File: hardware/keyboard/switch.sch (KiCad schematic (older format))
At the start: 136 parts

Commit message: I think im connecting the pins correctly on RGB...
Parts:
- added R1, R10, R11, R12, R13, R14, R2, R3, R4, R5, R6, R7, R8, R9: 10kR, symbol Device:R
- gave numbers to parts that had none: 136
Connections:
- net COL1: now also R1.1
- net COL10: now also R10.1
- net COL11: now also R11.1
- net COL12: now also R12.1
- net COL13: now also R13.1
- net COL14: now also R14.1
- net COL2: now also R2.1
- net COL3: now also R3.1
- net COL4: now also R4.1
- net COL5: now also R5.1
- net COL6: now also R6.1
- net COL7: now also R7.1
- net COL8: now also R8.1
- net COL9: now also R9.1
- new net 3.3V: R1.2, R10.2, R11.2, R12.2, R13.2, R14.2, R2.2, R3.2, R4.2, R5.2, R6.2, R7.2, R8.2, R9.2

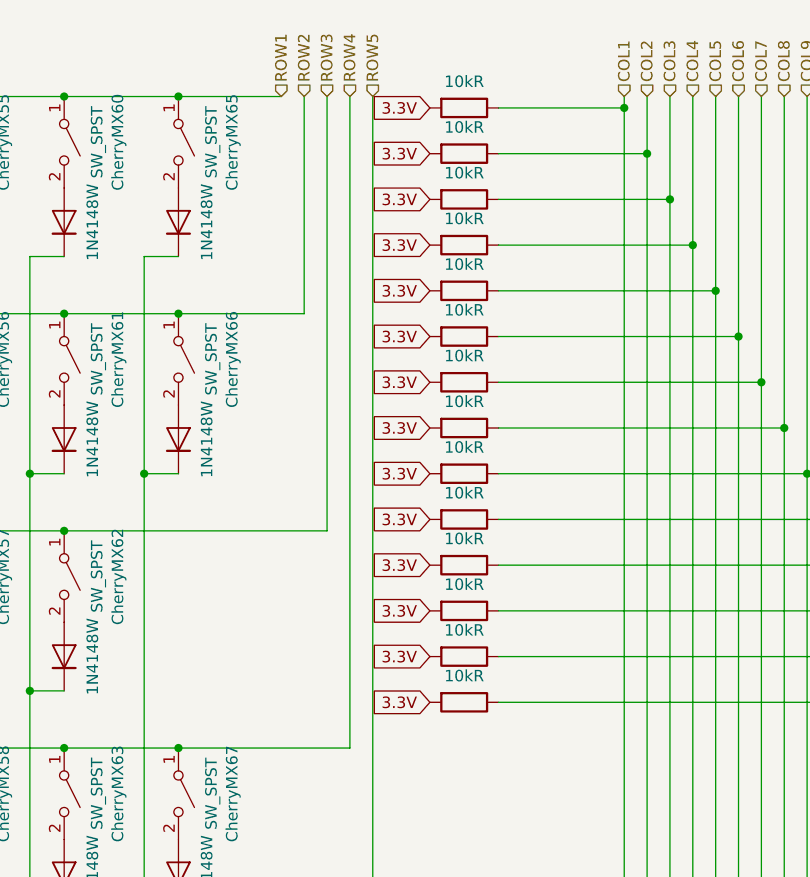
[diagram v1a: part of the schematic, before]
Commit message: switch to proper type of RGB(Common anode)
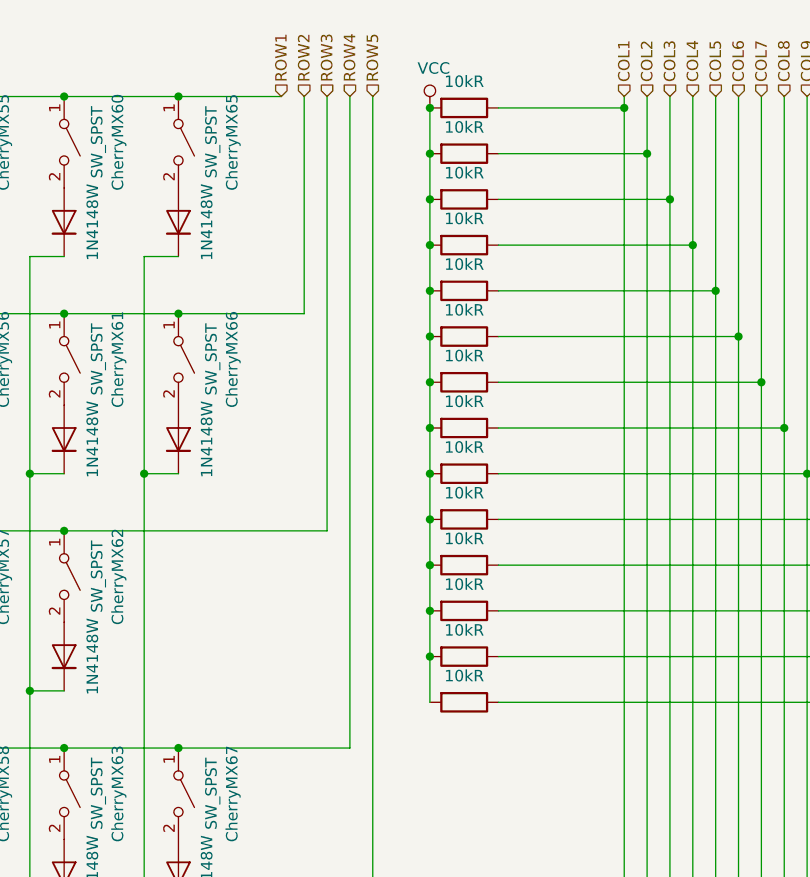
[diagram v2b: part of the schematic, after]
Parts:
- CherryMX1, CherryMX10, CherryMX11, CherryMX12, CherryMX13, CherryMX14, CherryMX15, CherryMX16, CherryMX17, CherryMX18, CherryMX19, CherryMX2, CherryMX20, CherryMX21, CherryMX22, CherryMX23, CherryMX24, CherryMX25, CherryMX26, CherryMX27, CherryMX28, CherryMX29, CherryMX3, CherryMX30, CherryMX31, CherryMX32, CherryMX33, CherryMX34, CherryMX35, CherryMX36, CherryMX37, CherryMX38, CherryMX39, CherryMX4, CherryMX40, CherryMX41, CherryMX42, CherryMX43, CherryMX44, CherryMX45, CherryMX46, CherryMX47, CherryMX48, CherryMX49, CherryMX5, CherryMX50, CherryMX51, CherryMX52, CherryMX53, CherryMX54, CherryMX55, CherryMX56, CherryMX57, CherryMX58, CherryMX59, CherryMX6, CherryMX60, CherryMX61, CherryMX62, CherryMX63, CherryMX64, CherryMX65, CherryMX66, CherryMX67, CherryMX68, CherryMX7, CherryMX8, CherryMX9: footprint (none) -> keyswitches:Kailh_socket_MX
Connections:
- net 3.3V renamed VCC

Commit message: use proper footprint, link symbols and footprints
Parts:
- CherryMX1, CherryMX10, CherryMX11, CherryMX12, CherryMX13, CherryMX14, CherryMX15, CherryMX16, CherryMX17, CherryMX18, CherryMX19, CherryMX2, CherryMX20, CherryMX21, CherryMX22, CherryMX23, CherryMX24, CherryMX25, CherryMX26, CherryMX27, CherryMX28, CherryMX29, CherryMX3, CherryMX30, CherryMX31, CherryMX32, CherryMX33, CherryMX34, CherryMX35, CherryMX36, CherryMX37, CherryMX38, CherryMX39, CherryMX4, CherryMX40, CherryMX41, CherryMX42, CherryMX43, CherryMX44, CherryMX45, CherryMX46, CherryMX47, CherryMX48, CherryMX49, CherryMX5, CherryMX50, CherryMX51, CherryMX52, CherryMX53, CherryMX54, CherryMX55, CherryMX56, CherryMX57, CherryMX58, CherryMX59, CherryMX6, CherryMX60, CherryMX61, CherryMX62, CherryMX63, CherryMX64, CherryMX65, CherryMX66, CherryMX67, CherryMX68, CherryMX7, CherryMX8, CherryMX9: footprint keyswitches:Kailh_socket_MX -> keyswitches:Kailh_socket_MX_optional_reversible; Footprint (none) -> keyswitches:Kailh_socket_MX_optional_reversible
- D1, D10, D11, D12, D13, D14, D15, D16, D17, D18, D19, D2, D20, D21, D22, D23, D24, D25, D26, D27, D28, D29, D3, D30, D31, D32, D33, D34, D35, D36, D37, D38, D39, D4, D40, D41, D42, D43, D44, D45, D46, D47, D48, D49, D5, D50, D51, D52, D53, D54, D55, D56, D57, D58, D59, D6, D60, D61, D62, D63, D64, D65, D66, D67, D68, D7, D8, D9: Footprint (none) -> Diode_SMD:D_SOD-123
- R1, R10, R11, R12, R13, R14, R2, R3, R4, R5, R6, R7, R8, R9: value 10kR -> 10k; footprint (none) -> Resistor_SMD:R_0603_1608Metric_Pad1.05x0.95mm_HandSolder; Footprint (none) -> Resistor_SMD:R_0603_1608Metric_Pad1.05x0.95mm_HandSolder; Value (none) -> 10k
